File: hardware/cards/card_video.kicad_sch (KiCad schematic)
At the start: 30 parts, among them J1 HDMI_A, J2 VGA HD15, M1 Core2350B (8MB PSRAM), U2 74LVC245A, U3 74LVC245A, U4 74LVC245A, U5 74LVC245A, U6 74LVC245A, U7 74LVC245A

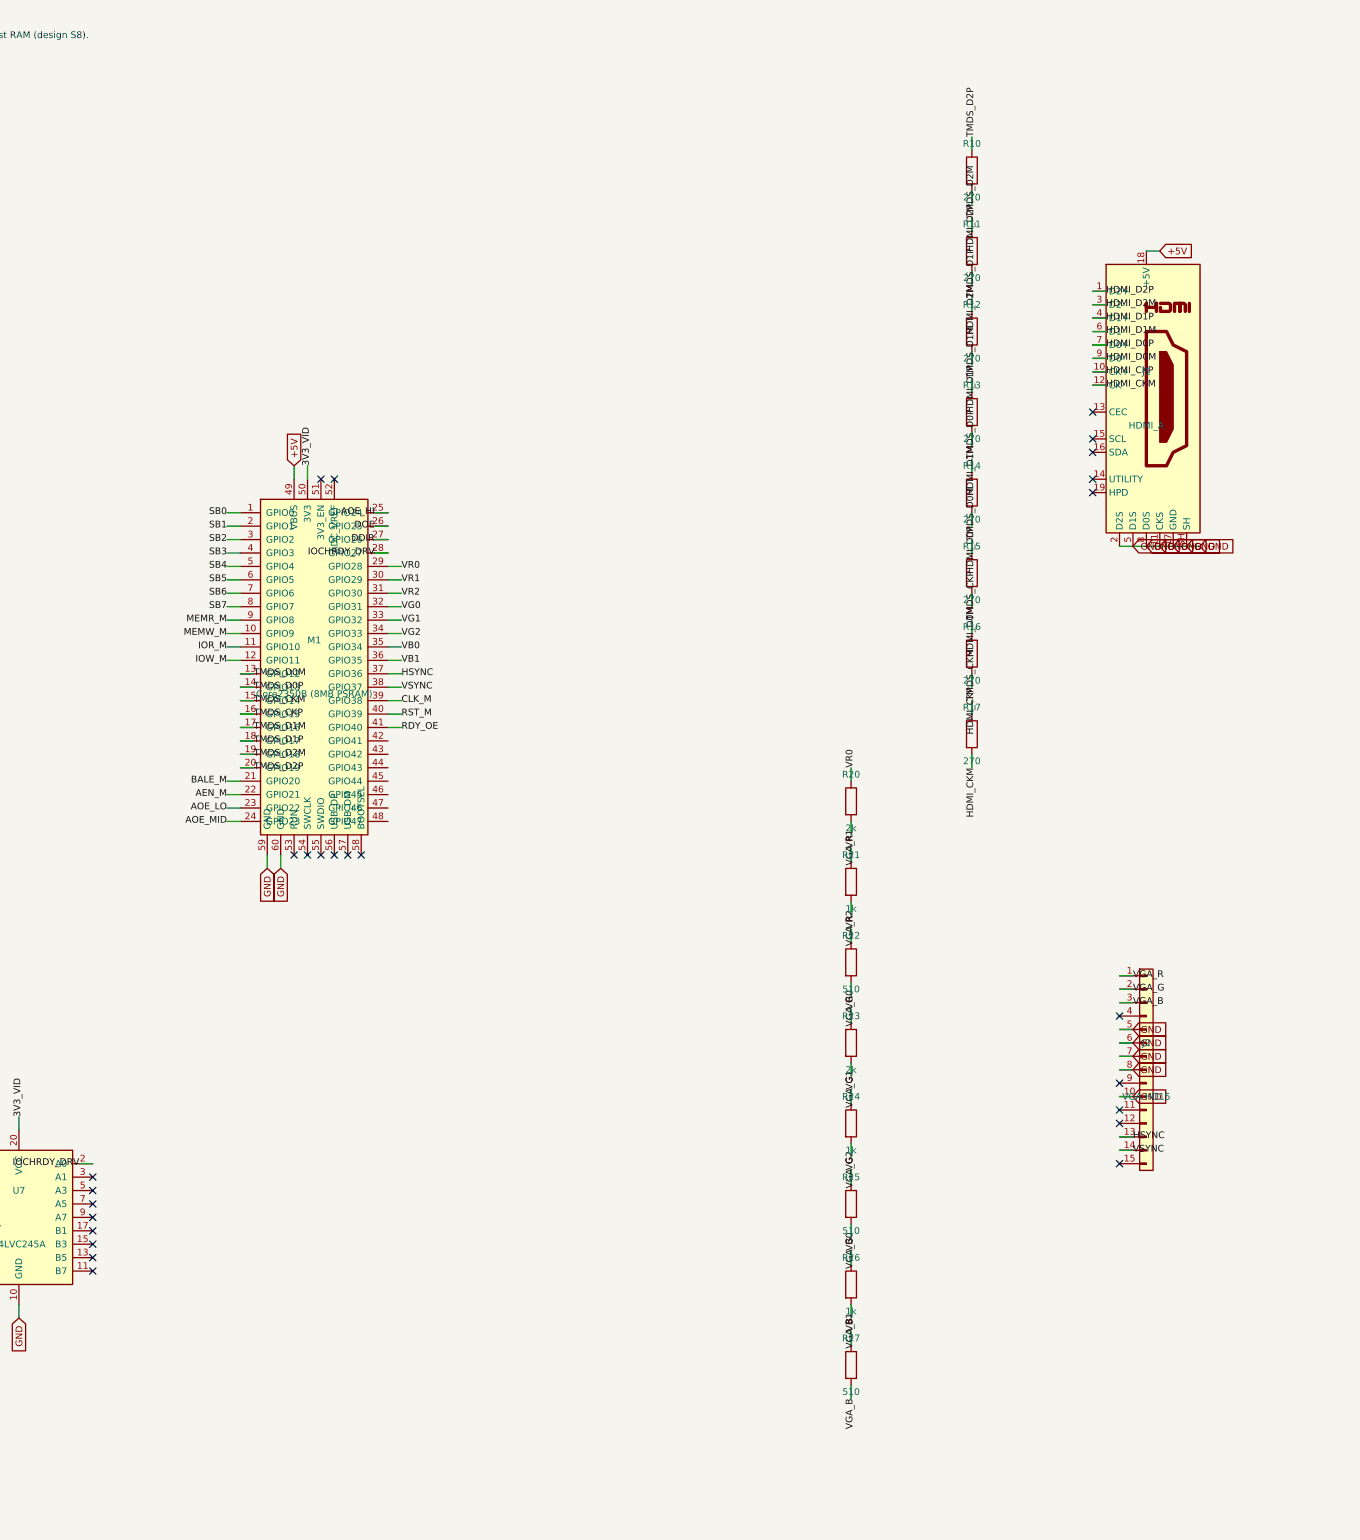
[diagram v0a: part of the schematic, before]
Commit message: Design review 2026-07-11: rail protection, decoupling, wiring fixes
Protection:
- Sidecar +5V now feeds through a 2A polyfuse into +5V_ISA with an
  SMBJ5.0A clamp + 22uF bulk (a faulted ISA card trips its own fuse
  instead of dropping the board; back-fed voltage is clamped).
- USB-C VBUS enters through a 3A polyfuse with an SMBJ5.0A on +5V
  (backstop for the CFG1 9-20V failure mode). CH224K gains a 1uF VDD
  cap; its PG routes to Supervisor GPIO16 as PD_PG. Buck output
  doubled to 2x22uF, 10uF at VIN, extra rail bulk.
- Supervisor USB-A host port: 27R series termination (RP2040
  requirement), USBLC6-2SC6 ESD array, 100uF VBUS bulk.
- Video: HDMI +5V fused (500mA), HPD sensed on GPIO41, 100R series on
  VGA sync. TMDS ESD array deferred to layout (no symbol).
- card_isatest: V5RAW bulk, Q1 gate soft-start cap, TVS on DUT rail.

Wiring fixes:
- SPKR had no driver anywhere (netlist: 1 node). Bus MCU GPIO22
  reassigned from the diagnostics-only bus-CLK sense to SPKR; bus_mcu
  drops CLK from its interface. Doc 5.2 updated.
- bus_mcu C8 decoupled +3V3, a rail that sheet never uses -> 3V3_BUS.
- Storage IRQ5 was push-pull (permanently driven when idle) -> 2N7002
  + gated '125 tri-state, same convention as the LPT IRQ7 stage.
- MAX3241 pump caps resized to the 5V datasheet values (47nF/330nF).
- LPT DB25 status inputs get 4.7k pull-ups (floated with no printer).
- Audio line-out gets a 100R series isolator before the jack.

Best practices:
- Decoupling to ~1x100nF per IC on every sheet + bulk per board
  (cpu_core 7->16 incl. the naked 3.3V oscillator, storage 4->11,
  parallel 6->13, rtc/com/video/bus_mcu/card_isatest similar).
- All floating spare CMOS inputs tied ('00/'74/'157/'02/'04/'125
  sections across cpu_core, bus_mcu, rtc, storage, card_isatest).

Sourcing: new parts mapped in parts.py with JLC-verified LCSC numbers;
Power_Protection lib registered in the tools; TPS563200 stock alert
(4 pcs left at JLC) flagged in parts.py + jlcpcb-sourcing.md. All
decisi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
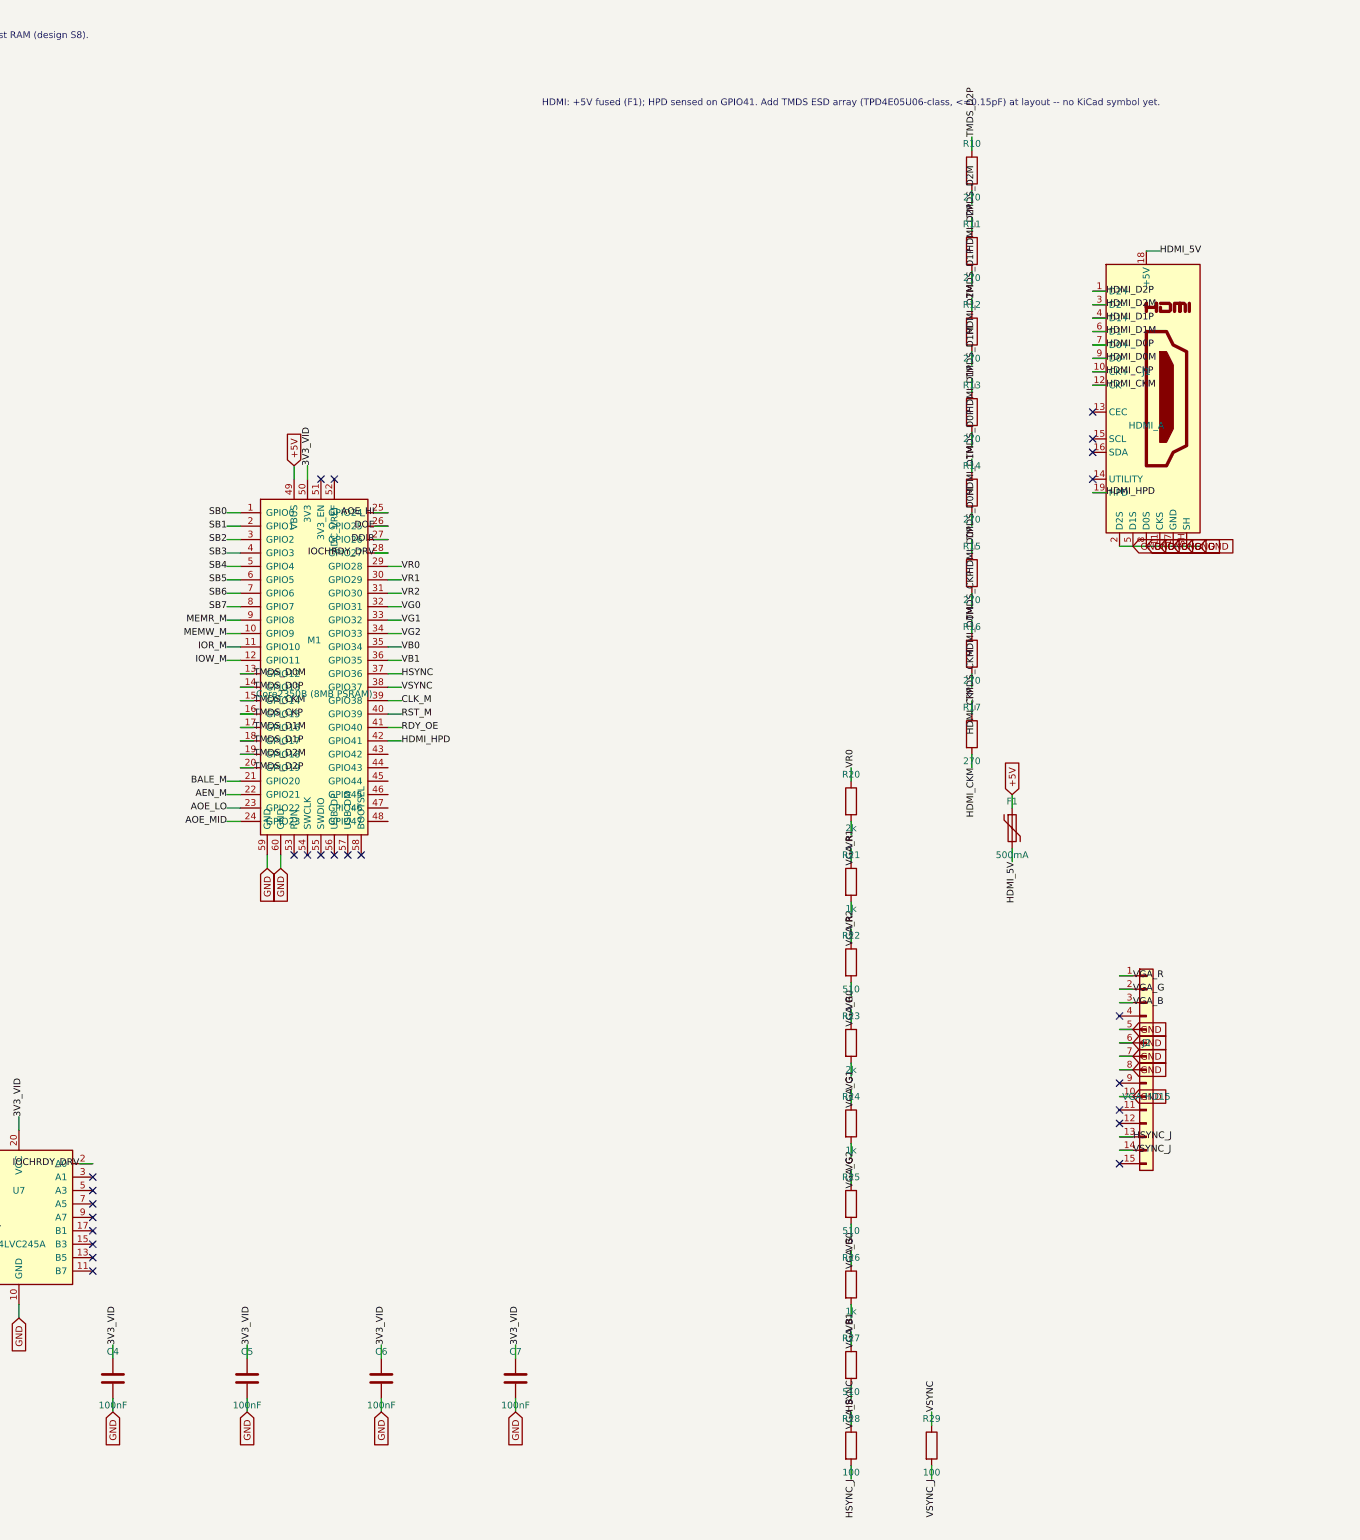
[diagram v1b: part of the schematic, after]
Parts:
- added C4, C5, C6, C7: 100nF, symbol Device:C
- added R13: 270, symbol Device:R
- added R28, R29: 100, symbol Device:R
- F1: renamed from R13; value 270 -> 500mA; symbol Device:R -> Device:Polyfuse; LCSC Part Num C22966 -> C46641014
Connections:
- net +5V: now also F1.1; no longer J1.18 (+5V)
- net 3V3_VID: now also C4.1, C5.1, C6.1, C7.1
- net GND: now also C4.2, C5.2, C6.2, C7.2
- net HDMI_D1M: now also R13.2; no longer F1.2
- net HSYNC: now also R28.1; no longer J2.13 (Pin_13)
- net TMDS_D1M: now also R13.1; no longer F1.1
- net VSYNC: now also R29.1; no longer J2.14 (Pin_14)
- net HDMI_HPD: now reaches M1.42 (GPIO41)
- net HDMI_HPD: now also J1.19 (HPD)
- new net HDMI_5V: F1.2, J1.18 (+5V)
- new net HSYNC_J: J2.13 (Pin_13), R28.2
- new net VSYNC_J: J2.14 (Pin_14), R29.2
- no-connect marks 42 -> 41
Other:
- note added: "HDMI: +5V fused (F1); HPD sensed on GPIO41. Add TMDS ESD array (TPD4E05U06-class, <=0.15pF) at layout -- no KiCad symbol yet."

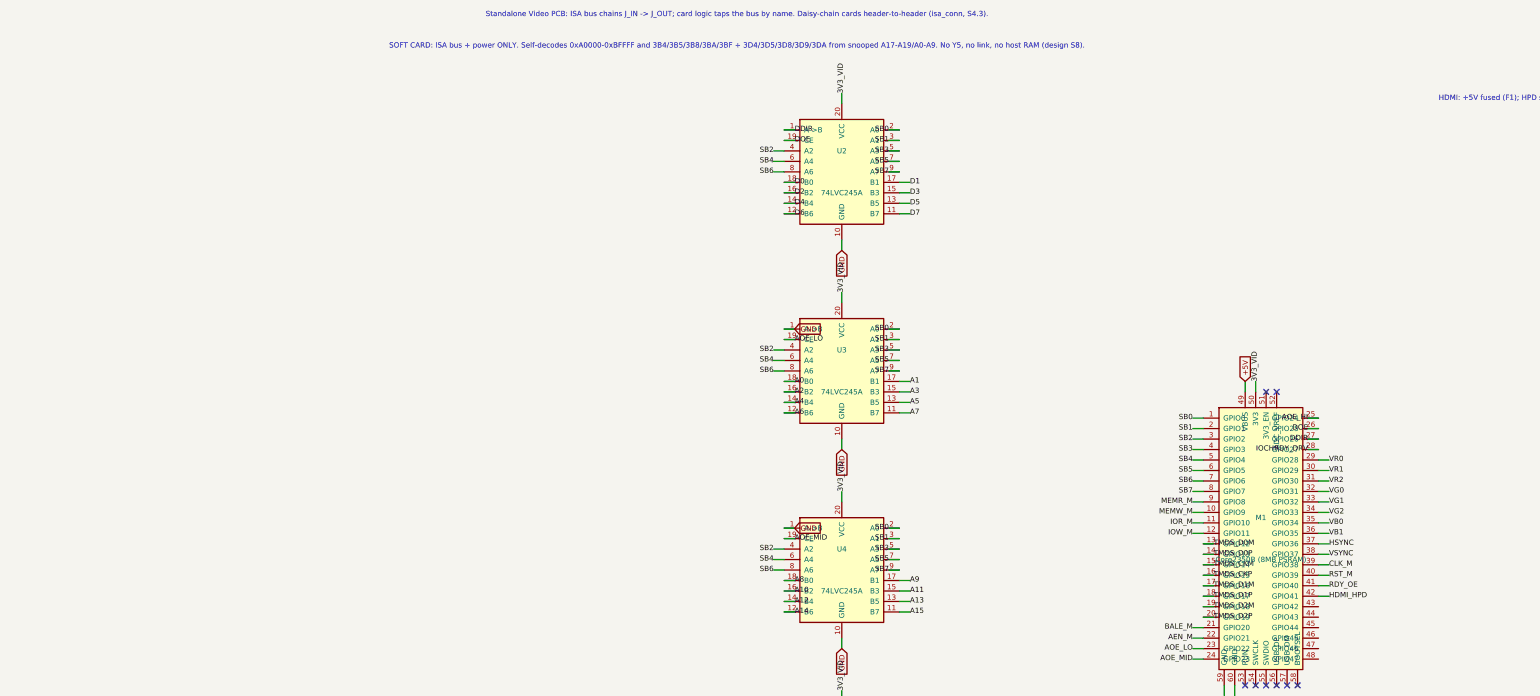
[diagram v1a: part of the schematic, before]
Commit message: Storage/video: enable + base-address straps
Completes the jumper story started with COM/LPT: every on-board peripheral
can now be disabled or re-strapped to make room for the same card on the
sidecar chain.

- storage: JP1 base 0x300/0x320 (differ only in A5; A5_SEL replaces nA5 in
  the HI_MATCH tree, XTIDE UB supports both) and JP2 enable on DEC1's spare
  ~E1 (open kills /CS0 + /ODD_SEL, so DEC2/DEC3, both high-byte latches and
  the low-byte '245 go inert; INTRQ's pull-down keeps IRQ5 released). Same
  pattern as the LPT sheet.
- video: firmware-read boot straps -- this snoop card decodes in firmware,
  so there is no hardware chip-select to gate. JP1/VID_EN (GPIO42, 10k to
  3V3_VID) open = firmware keeps every bus-facing OE off (all drivers are
  MCU-gated tri-states, so a disabled card is electrically silent);
  JP2/VID_BASE (GPIO43) closed = CGA windows (0x3D4/0xB8000), open =
  MDA/Hercules (0x3B4/0xB0000) -- the snoop equivalent of a period card's
  MDA/CGA switch.

Design doc updated (8, 10, 14 I/O map); decisions logged in
questions-storage.md / questions-video.md.

Verified: motherboard + cards rebuild with zero structural ERC; netlist
ties each strap to its jumper, pull resistor and decode/GPIO pin
(A5_SEL/~{STOR_EN} on storage, VID_EN/VID_BASE on the video module).

Co-Authored-By: Claude Fable 5 <noreply@anthropic.com>
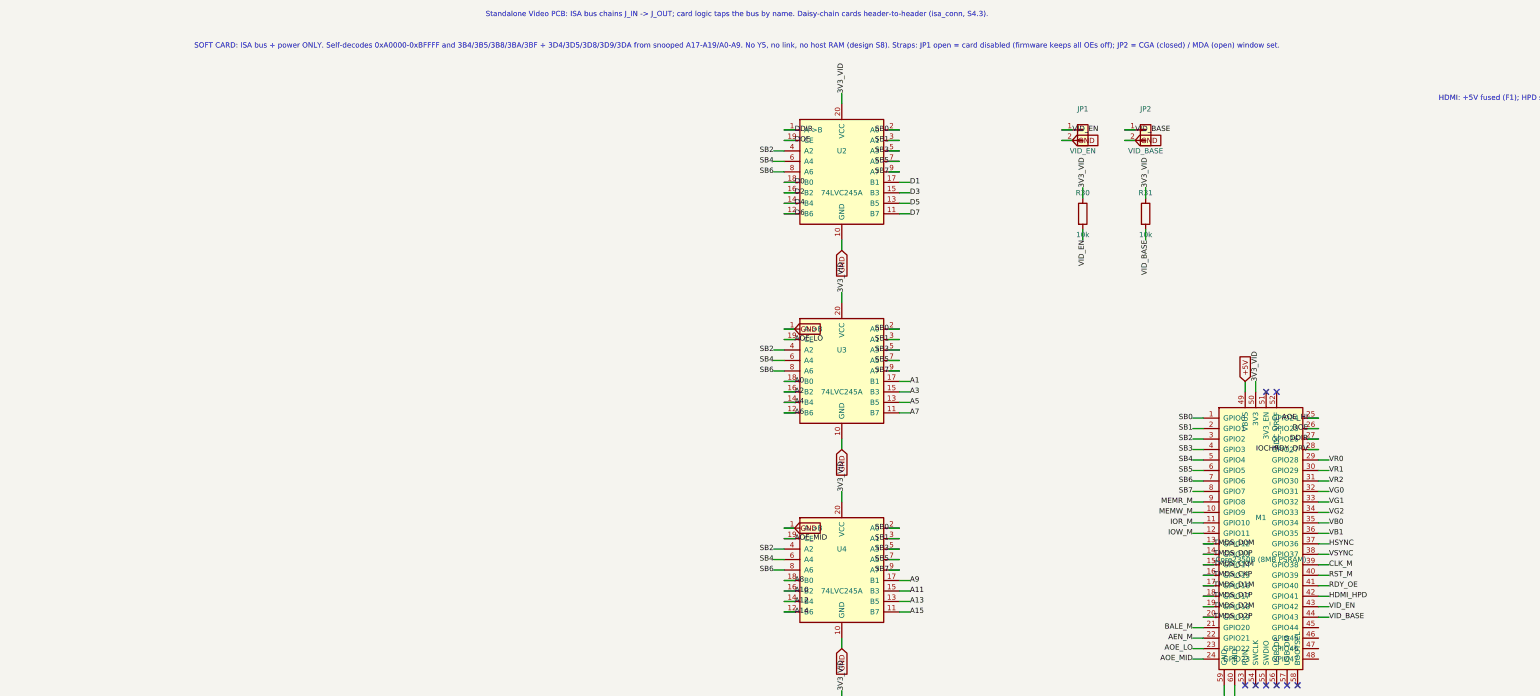
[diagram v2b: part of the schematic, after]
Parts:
- added JP1: VID_EN, symbol Connector_Generic:Conn_01x02
- added JP2: VID_BASE, symbol Connector_Generic:Conn_01x02
- added R30, R31: 10k, symbol Device:R
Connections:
- net 3V3_VID: now also R30.1, R31.1
- net GND: now also JP1.2 (Pin_2), JP2.2 (Pin_2)
- net VID_EN: now reaches M1.43 (GPIO42)
- net VID_EN: now also JP1.1 (Pin_1), R30.2
- net VID_BASE: now reaches M1.44 (GPIO43)
- net VID_BASE: now also JP2.1 (Pin_1), R31.2
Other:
- note added: "SOFT CARD: ISA bus + power ONLY. Self-decodes 0xA0000-0xBFFFF and 3B4/3B5/3B8/3BA/3BF + 3D4/3D5/3D8/3D9/3DA from snooped A17-A19/A0-A9. No Y5, no link, no host RAM (design S8). Straps: JP1 open = card disabled (firmware keeps all OEs off); JP2 = CGA (closed) / MDA (open) window set."
- note removed: "SOFT CARD: ISA bus + power ONLY. Self-decodes 0xA0000-0xBFFFF and 3B4/3B5/3B8/3BA/3BF + 3D4/3D5/3D8/3D9/3DA from snooped A17-A19/A0-A9. No Y5, no link, no host RAM (design S8)."
